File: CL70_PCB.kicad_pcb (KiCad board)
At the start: 2 copper layers, 204 parts, among them J1 AVR-ISP-6, SW1 SW_Push, U1 ATmega32U4-MU, U2 PRTR5V0U2X, Y1 16MHz

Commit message: Realignment footprint
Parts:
- moved C5 52.3 mm to (341.3, 150.0), turned to -90 degrees
- moved C4 47.6 mm to (345.3, 139.8), turned to -90 degrees
- moved C1 44.5 mm to (349.2, 138.9)
- moved C6 41.6 mm to (352.4, 153.2)
- moved C7 37.4 mm to (355.5, 142.9)
- moved C2 34.8 mm to (361.1, 146.8), turned to 0 degrees
- moved C3 34.5 mm to (361.1, 149.2), turned to 0 degrees
- moved RC8 33.2 mm to (342.0, 153.9), turned to 180 degrees
- moved D71 10.3 mm to (377.0, 164.2)
- moved D32 6.20 mm to (337.3, 134.1)
- moved D68 6.20 mm to (327.8, 191.2)
- moved D69 6.20 mm to (346.9, 191.2)
- moved D47 6.16 mm to (330.2, 153.1)
- moved D60 6.10 mm to (346.9, 172.2)
- moved J1 3.27 mm to (356.7, 168.1)
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
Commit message: Add PCB outline
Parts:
- moved C2 0.91 mm to (360.2, 146.8)
- moved C3 0.91 mm to (360.2, 149.2)
- moved Y1 0.91 mm to (355.5, 147.9)
- moved USB1 0.46 mm to (350.1, 95.8)
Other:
- board outline added: 343.8 x 98.1 mm
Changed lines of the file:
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@@
 	(footprint "locallib:C_0603"
 		(layer "B.Cu")
-		(at 361.1 149.225)
+		(at 360.19375 149.225)
 		(descr "Capacitor SMD 0603, reflow soldering, AVX (see smccp.pdf)")
 		(tags "capacitor 0603")
@@
 	(footprint "locallib:C_0603"
 		(layer "B.Cu")
-		(at 361.1 146.84375)
+		(at 360.19375 146.84375)
 		(descr "Capacitor SMD 0603, reflow soldering, AVX (see smccp.pdf)")
 		(tags "capacitor 0603")
@@
 	(footprint "Crystal:Crystal_SMD_3225-4Pin_3.2x2.5mm"
 		(layer "B.Cu")
-		(at 356.45 147.94375 90)
+		(at 355.54375 147.94375 90)
 		(descr "SMD3225/4, Crystal, 3.2x2.5mm package, SMD, generated with kicad-footprint-generator make_crystal.py, http://www.txccrystal.com/images/pdf/7m-accuracy.pdf")
 		(property "Reference" "Y1"
@@
 	(footprint "Type-C:HRO-TYPE-C-31-M-12-Assembly"
 		(layer "B.Cu")
-		(at 350.04375 95.35)
+		(at 350.05 95.805)
 		(property "Reference" "USB1"
 			(at 0 9.25 0)
@@
 		(layer "Dwgs.User")
 	)
+	(gr_arc
+		(start 371.475 146.75)
+		(mid 383.475004 158.750002)
+		(end 371.475 170.75)
+		(stroke
+			(width 0.2)
+			(type default)
+		)
+		(layer "Edge.Cuts")
+	)
+	(gr_arc
+		(start 354.421762 97.2107)
+		(mid 354.983056 97.443195)
+		(end 355.21555 98.004492)
+		(stroke
+			(width 0.2)
+			(type default)
+		)
+		(layer "Edge.Cuts")
+	)
+	(gr_line
+		(start 39.6875 192.88125)
+		(end 39.6875 105.568812)
+		(stroke
+			(width 0.2)
+			(type default)
+		)
+		(layer "Edge.Cuts")
+	)
+	(gr_arc
+		(start 344.87195 98.004592)
+		(mid 345.104451 97.443225)
+		(end 345.665762 97.21078)
+		(stroke
+			(width 0.2)
+			(type default)
+		)
+		(layer "Edge.Cuts")
+	)
+	(gr_arc
+		(start 39.6875 105.568812)
+		(mid 40.384966 103.884975)
+		(end 42.068812 103.1875)
+		(stroke
+			(width 0.2)
+			(type default)
+		)
+		(layer "Edge.Cuts")
+	)
+	(gr_arc
+		(start 369.8875 192.881292)
+		(mid 369.190062 194.565071)
+		(end 367.50625 195.2625)
+		(stroke
+			(width 0.2)
+			(type default)
+		)
+		(layer "Edge.Cuts")
+	)
+	(gr_line
+		(start 345.665762 97.2107)
+		(end 354.421762 97.2107)
+		(stroke
+			(width 0.2)
+			(type default)
+		)
+		(layer "Edge.Cuts")
+	)
+	(gr_arc
+		(start 344.87195 101.599992)
+		(mid 344.406978 102.722523)
+		(end 343.28445 103.1875)
+		(stroke
+			(width 0.2)
+			(type default)
+		)
+		(layer "Edge.Cuts")
+	)
+	(gr_line
+		(start 343.28445 103.1875)
+		(end 42.068812 103.1875)
+		(stroke
+			(width 0.2)
+			(type default)
+		)
+		(layer "Edge.Cuts")
+	)
+	(gr_line
+		(start 369.8875 172.337492)
+		(end 369.8875 192.881292)
+		(stroke
+			(width 0.2)
+			(type default)
+		)
+		(layer "Edge.Cuts")
+	)
+	(gr_line
+		(start 345.665762 97.21078)
+		(end 345.665762 97.2107)
+		(stroke
+			(width 0.2)
+			(type default)
+		)
+		(layer "Edge.Cuts")
+	)
+	(gr_arc
+		(start 356.803062 103.1875)
+		(mid 355.680523 102.722528)
+		(end 355.21555 101.599992)
+		(stroke
+			(width 0.2)
+			(type default)
+		)
+		(layer "Edge.Cuts")
+	)
+	(gr_arc
+		(start 367.506262 103.1875)
+		(mid 369.190071 103.884945)
+		(end 369.8875 105.56875)
+		(stroke
+			(width 0.2)
+			(type default)
+		)
+		(layer "Edge.Cuts")
+	)
+	(gr_arc
+		(start 371.475 146.75)
+		(mid 370.352441 146.285046)
+		(end 369.8875 145.1625)
+		(stroke
+			(width 0.2)
+			(type default)
+		)
+		(layer "Edge.Cuts")
+	)
+	(gr_line
+		(start 344.87195 101.599992)
+		(end 344.87195 98.004592)
+		(stroke
+			(width 0.2)
+			(type default)
+		)
+		(layer "Edge.Cuts")
+	)
+	(gr_line
+		(start 42.068762 195.2625)
+		(end 367.50625 195.2625)
+		(stroke
+			(width 0.2)
+			(type default)
+		)
+		(layer "Edge.Cuts")
+	)
+	(gr_line
+		(start 355.21555 98.004492)
+		(end 355.21555 101.599992)
+		(stroke
+			(width 0.2)
+			(type default)
+		)
+		(layer "Edge.Cuts")
+	)
+	(gr_arc
+		(start 42.068762 195.2625)
+		(mid 40.384954 194.565047)
+		(end 39.6875 192.88125)
+		(stroke
+			(width 0.2)
+			(type default)
+		)
+		(layer "Edge.Cuts")
+	)
+	(gr_arc
+		(start 369.8875 172.337492)
+		(mid 370.352467 171.214976)
+		(end 371.475 170.75)
+		(stroke
+			(width 0.2)
+			(type default)
+		)
+		(layer "Edge.Cuts")
+	)
+	(gr_line
+		(start 367.506262 103.1875)
+		(end 356.803062 103.1875)
+		(stroke
+			(width 0.2)
+			(type default)
+		)
+		(layer "Edge.Cuts")
+	)
+	(gr_line
+		(start 369.8875 105.56875)
+		(end 369.8875 145.1625)
+		(stroke
+			(width 0.2)
+			(type default)
+		)
+		(layer "Edge.Cuts")
+	)
 	(group ""
 		(members "01f0b98f-9fbf-4339-9750-24d2992556fd" "0355ff27-1e74-4531-91ec-7afcd7ec99a2"
@@
 		)
 	)
+	(group ""
+		(members "0e2a9951-a378-4da8-98fe-729fd5110501" "11c98efb-e5c4-4a83-9d8d-b93e626b395c"
+			"19e8fbd3-0d80-4f89-bcad-f88af3cd8026" "2a881e81-64bd-49b1-8f18-b7fc72406794"
+			"2c628242-99f6-44d3-804e-fae6e092cd84" "36ff1723-645c-4ea2-a89e-666fb6f61650"
+			"40e42480-0976-4067-8680-fe6dd074dff7" "46f23a6b-3d0c-4e92-805b-4b3b9c2d146e"
+			"47799a47-71c1-41d2-be0c-02f1f8502c5b" "6a57dcbe-f917-4bf4-afba-9318e853d4c9"
+			"6dfccded-3a9c-4300-a0bb-f29846b9b758" "7f1c7e5f-c4c1-428b-bafd-2ee28e34fea0"
+			"8342ee14-e821-4a54-89ae-72e6da792c9f" "b58aadb1-8298-497d-8d19-9d3c9efc98b3"
+			"bbc2a745-2ae9-4e90-8fd2-8394d0d31e88" "bf7335ba-ab35-49f0-846f-eec9758f1bc8"
+			"ca3899e7-4a94-421b-8d8c-8840a08a6e91" "df78106b-4ed4-4e74-bcb2-cc24398d9495"
+			"e9bb1a92-d6f3-49a2-afdc-1b0c10f2b2ad" "ee82f6a7-5d3c-43cf-abe7-82fa5f20290f"
+			"f653473b-249b-42f0-b5a5-de18ca18a995"
+		)
+	)

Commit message: Add wiring
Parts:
- RC1, RC2: value 22 -> 22k
- RLED1, RLED2, RLED3: value 1k -> 330
- moved SW1 19.4 mm to (361.9, 140.8), turned to 0 degrees
- moved D71 15.6 mm to (365.8, 153.4)
- moved RC3 14.2 mm to (355.4, 139.8), turned to 0 degrees
- moved CRGB12 12.6 mm to (187.2, 176.3)
- moved CRGB5 12.4 mm to (187.0, 119.9)
- moved CRGB8 12.3 mm to (61.5, 120.2)
- moved CRGB7 12.2 mm to (103.5, 119.9)
- moved CRGB11 12.2 mm to (144.8, 177.4)
- moved CRGB6 12.2 mm to (144.8, 119.9)
- moved CRGB10 12.0 mm to (103.2, 177.1)
- moved J1 5.12 mm to (356.7, 163.0)
- moved C2 2.43 mm to (360.7, 149.2)
- moved C3 2.42 mm to (360.6, 146.8)
- moved C8 1.64 mm to (365.6, 171.5)
- moved C9 1.55 mm to (365.6, 169.9)
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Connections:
- RC4 pad 1: Net-(U1-PD0) -> Net-(U1-PD2)
- RC4 pad 2: RESW_A -> RESW_B
- RC5 pad 2: RESW_B -> RESW_A
- S47 pad 1: COL8 -> COL7
- U1 pad 18: Net-(U1-PD0) -> ROW7
- U1 pad 20: ROW9 -> Net-(U1-PD2)
- U1 pad 22: ROW7 -> ROW9
- U1 pad 26: ROW5 -> ROW4
- U1 pad 27: ROW4 -> ROW5
- U1 pad 28: ROW3 -> ROW2
- U1 pad 29: ROW2 -> ROW3
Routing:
- net GND: track 0.00 -> 912.2 mm, vias 0 -> 6
- net +5V: track 0.00 -> 788.4 mm, vias 0 -> 12
- net COL2: track 0.00 -> 469.4 mm, vias 0 -> 1
- net COL1: track 0.00 -> 462.7 mm, vias 0 -> 2
- net COL3: track 0.00 -> 432.4 mm, vias 0 -> 2
- net COL0: track 0.00 -> 421.0 mm, vias 0 -> 1
- net ROW0: track 0.00 -> 400.1 mm, vias 0 -> 4
- net COL4: track 0.00 -> 375.7 mm, vias 0 -> 2
- net ROW3: track 0.00 -> 364.2 mm, vias 0 -> 2
- net ROW1: track 0.00 -> 355.6 mm, vias 0 -> 2
- net ROW8: track 0.00 -> 353.8 mm
- net SLOCK_IND: track 0.00 -> 353.0 mm, vias 0 -> 2
- net CAPS_IND: track 0.00 -> 349.4 mm, vias 0 -> 2
- net LAYER_IND: track 0.00 -> 342.4 mm, vias 0 -> 2
- net ROW2: track 0.00 -> 340.6 mm
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
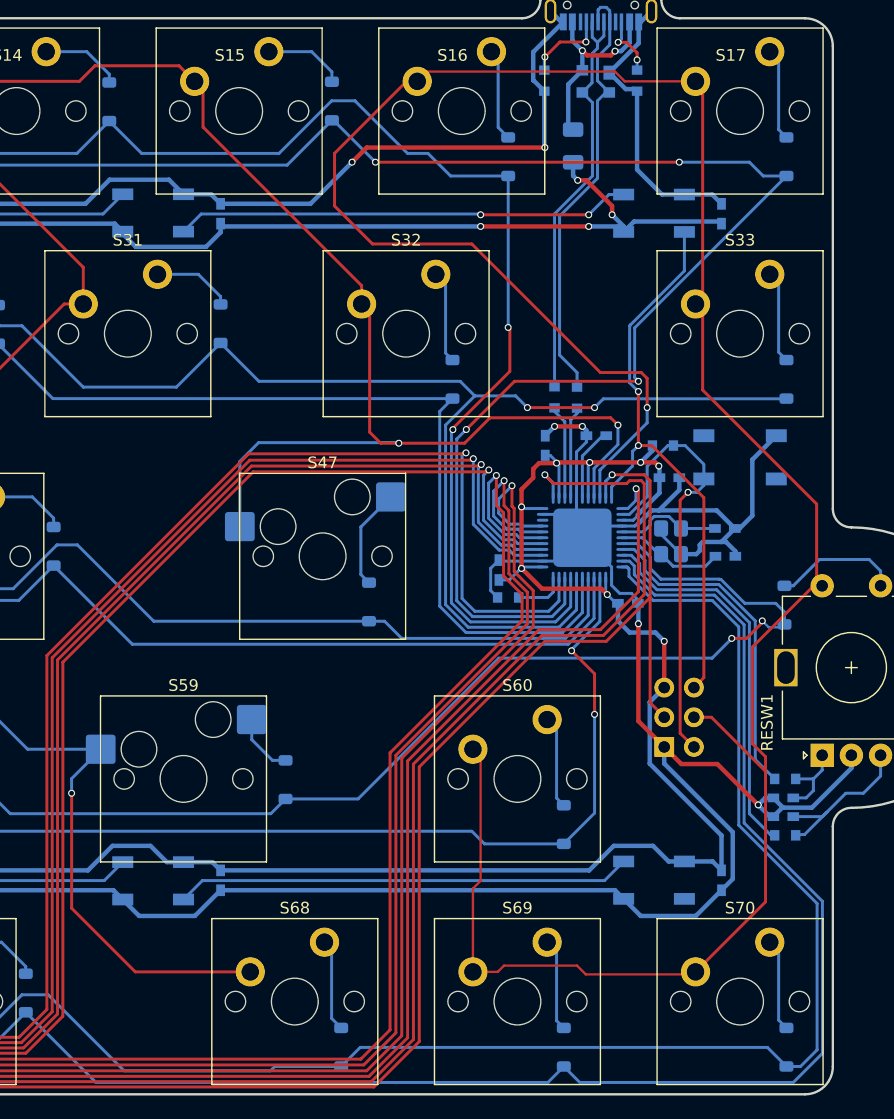
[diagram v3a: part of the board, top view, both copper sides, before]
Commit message: Add graphic sorder mask
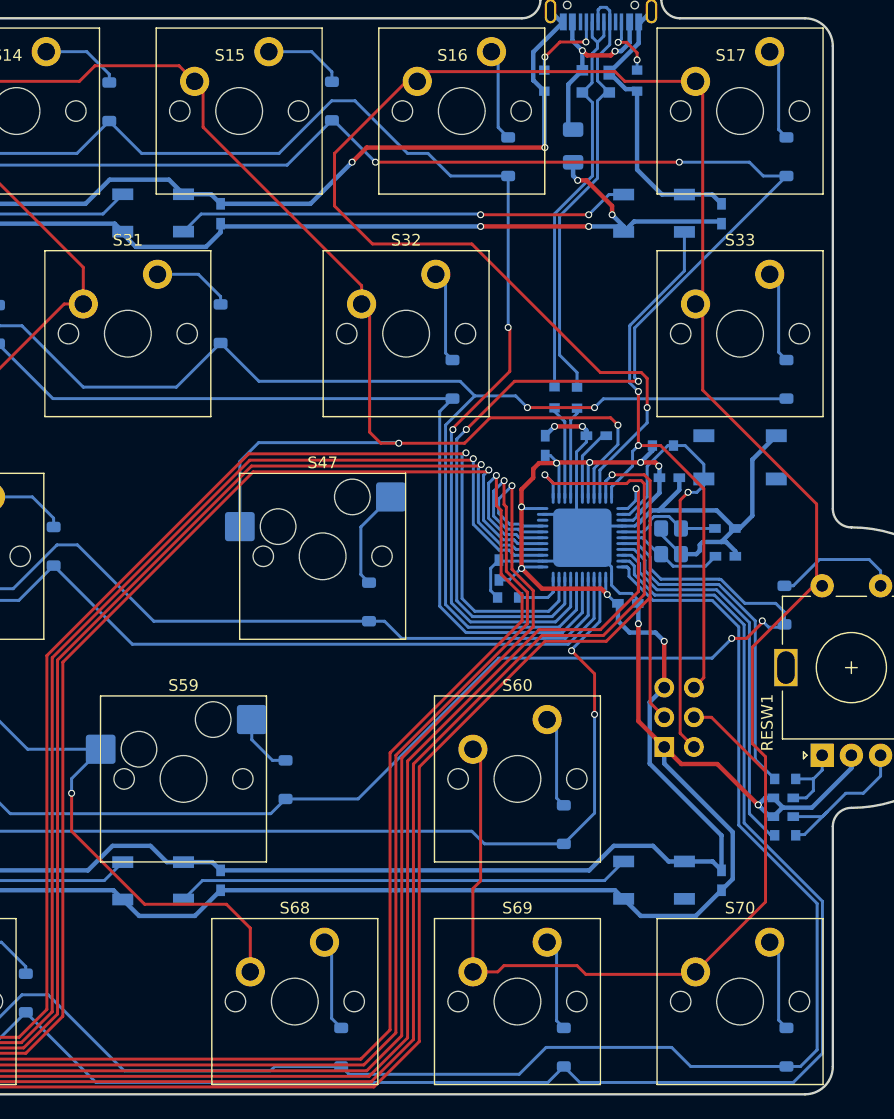
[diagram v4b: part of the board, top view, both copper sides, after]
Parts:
- added G***: LOGO, Graphics:SURVEY_CORPS, F.Cu at (309.5, 187.3)
- added G***: LOGO, Graphics:PCB_INFO, B.Cu at (269.9, 158.2)
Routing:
- net COL7: track 216.5 -> 214.8 mm
- net ROW9: track 334.8 -> 335.4 mm
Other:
- board text added: "+"
- board text added: "-"

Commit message: Add production files
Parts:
- RC1, RC2: value 22k -> 22
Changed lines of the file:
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@@
 		(tenting front back)
 		(pcbplotparams
-			(layerselection 0x00000000_00000000_55555555_5755f5ff)
+			(layerselection 0x00000000_00000000_55555555_5755f5df)
 			(plot_on_all_layers_selection 0x00000000_00000000_00000000_00000000)
 			(disableapertmacros no)
@@
 			(outputformat 1)
 			(mirror no)
-			(drillshape 1)
+			(drillshape 0)
 			(scaleselection 1)
-			(outputdirectory "")
+			(outputdirectory "Production/Gerber/")
 		)
 	)
@@
 			)
 		)
-		(property "Value" "22k"
+		(property "Value" "22"
 			(at 0 -1.5 90)
 			(layer "B.Fab")
@@
 			)
 		)
-		(property "Value" "22k"
+		(property "Value" "22"
 			(at 0 -1.5 90)
 			(layer "B.Fab")
@@
 		(start 61.11875 188.9125)
 		(end 62.4125 188.9125)
-		(width 0.254)
+		(width 0.381)
 		(layer "B.Cu")
 		(net 89)
@@
 		(start 53.6875 182.5625)
 		(end 50 178.875)
-		(width 0.254)
+		(width 0.381)
 		(layer "B.Cu")
 		(net 92)
@@
 		(start 50 175.73)
 		(end 48.895 174.625)
-		(width 0.254)
+		(width 0.381)
 		(layer "B.Cu")
 		(net 92)
@@
 		(start 50 178.875)
 		(end 50 175.73)
-		(width 0.254)
+		(width 0.381)
 		(layer "B.Cu")
 		(net 92)
@@
 		(start 59.31875 182.5625)
 		(end 53.6875 182.5625)
-		(width 0.254)
+		(width 0.381)
 		(layer "B.Cu")
 		(net 92)
@@
 		(start 59.31875 185.7375)
 		(end 53.66375 185.7375)
-		(width 0.254)
+		(width 0.381)
 		(layer "B.Cu")
 		(net 93)
@@
 		(start 53.66375 185.7375)
 		(end 48.895 180.96875)
-		(width 0.254)
+		(width 0.381)
 		(layer "B.Cu")
 		(net 93)
@@
 		(start 53.6625 188.9125)
 		(end 52.0625 187.3125)
-		(width 0.254)
+		(width 0.381)
 		(layer "B.Cu")
 		(net 94)
@@
 		(start 52.0625 187.3125)
 		(end 48.895 187.3125)
-		(width 0.254)
+		(width 0.381)
 		(layer "B.Cu")
 		(net 94)
@@
 		(start 59.31875 188.9125)
 		(end 53.6625 188.9125)
-		(width 0.254)
+		(width 0.381)
 		(layer "B.Cu")
 		(net 94)
@@
 		(start 61.11875 182.5625)
 		(end 62.4375 182.5625)
-		(width 0.254)
+		(width 0.381)
 		(layer "B.Cu")
 		(net 122)
@@
 		(start 61.11875 185.7375)
 		(end 62.4875 185.7375)
-		(width 0.254)
+		(width 0.381)
 		(layer "B.Cu")
 		(net 123)
@@
 	)
 	(segment
-		(start 341.75 142.767359)
-		(end 341.75 144.8)
-		(width 0.254)
-		(layer "F.Cu")
-		(net 125)
-	)
-	(segment
 		(start 68.2125 108)
 		(end 77 108)
@@
 	)
 	(segment
-		(start 332.5 166.25)
-		(end 332.5 190)
+		(start 332.5 190)
+		(end 329.75 192.75)
 		(width 0.254)
 		(layer "F.Cu")
@@
 	)
 	(segment
-		(start 329.75 192.75)
-		(end 96.5 192.75)
+		(start 343.75 152.3)
+		(end 343.75 155)
 		(width 0.254)
 		(layer "F.Cu")
@@
 	)
 	(segment
-		(start 341.760686 142.756673)
-		(end 341.75 142.767359)
+		(start 94.5 190.75)
+		(end 94.5 185.46375)
+		(width 0.254)
+		(layer "F.Cu")
+		(net 125)
+	)
+	(segment
+		(start 94.5 185.46375)
+		(end 93.82125 184.785)
 		(width 0.254)
 		(layer "F.Cu")
@@
 	)
 	(segment
-		(start 93.82125 190.07125)
-		(end 93.82125 184.785)
+		(start 96.5 192.75)
+		(end 94.5 190.75)
+		(width 0.254)
+		(layer "F.Cu")
+		(net 125)
+	)
+	(segment
+		(start 341.760686 142.756673)
+		(end 341.75 142.767359)
 		(width 0.254)
 		(layer "F.Cu")
@@
 	)
 	(segment
-		(start 96.5 192.75)
-		(end 93.82125 190.07125)
+		(start 341.75 142.767359)
+		(end 341.75 144.8)
 		(width 0.254)
 		(layer "F.Cu")
@@
 	)
 	(segment
-		(start 341.95 145)
-		(end 341.95 150.5)
+		(start 77.75 107.25)
+		(end 85.3425 107.25)
 		(width 0.254)
 		(layer "F.Cu")
@@
 	)
 	(segment
-		(start 341.95 150.5)
-		(end 343.75 152.3)
+		(start 84.5 184.25)
+		(end 85.035 184.785)
 		(width 0.254)
 		(layer "F.Cu")
@@
 	)
 	(segment
-		(start 332.5 190)
-		(end 329.75 192.75)
+		(start 70 168.5)
+		(end 68.5 170)
 		(width 0.254)
 		(layer "F.Cu")
@@
 	)
 	(segment
-		(start 77.75 107.25)
-		(end 85.3425 107.25)
+		(start 341.75 144.8)
+		(end 341.95 145)
 		(width 0.254)
 		(layer "F.Cu")
@@
 	)
 	(segment
-		(start 84.5 184.25)
-		(end 85.035 184.785)
+		(start 85.3425 107.25)
+		(end 86.6775 108.585)
 		(width 0.254)
 		(layer "F.Cu")
@@
 	)
 	(segment
-		(start 70 168.5)
-		(end 68.5 170)
+		(start 77 108)
+		(end 77.75 107.25)
 		(width 0.254)
 		(layer "F.Cu")
@@
 	)
 	(segment
-		(start 85.3425 107.25)
-		(end 86.6775 108.585)
+		(start 72.39 128.89)
+		(end 73.25 129.75)
 		(width 0.254)
 		(layer "F.Cu")
@@
 	)
 	(segment
-		(start 77 108)
-		(end 77.75 107.25)
+		(start 73.25 145.16375)
+		(end 74.77125 146.685)
 		(width 0.254)
 		(layer "F.Cu")
@@
 	)
 	(segment
-		(start 343.75 152.3)
-		(end 343.75 155)
+		(start 70.54375 184.25)
+		(end 84.5 184.25)
 		(width 0.254)
 		(layer "F.Cu")
@@
 	)
 	(segment
-		(start 72.39 128.89)
-		(end 73.25 129.75)
+		(start 72.39 127.635)
+		(end 72.39 128.89)
 		(width 0.254)
 		(layer "F.Cu")
@@
 	)
 	(segment
-		(start 341.75 144.8)
-		(end 341.95 145)
+		(start 332.5 166.25)
+		(end 332.5 190)
 		(width 0.254)
 		(layer "F.Cu")
@@
 	)
 	(segment
-		(start 73.25 145.16375)
-		(end 74.77125 146.685)
+		(start 91.885 127.635)
+		(end 96.2025 127.635)
 		(width 0.254)
 		(layer "F.Cu")
@@
 	)
 	(segment
-		(start 70.54375 184.25)
-		(end 84.5 184.25)
+		(start 68.5 170)
+		(end 68.5 183.27625)
 		(width 0.254)
 		(layer "F.Cu")
@@
 	)
 	(segment
-		(start 72.39 127.635)
-		(end 72.39 128.89)
+		(start 329.75 192.75)
+		(end 96.5 192.75)
 		(width 0.254)
 		(layer "F.Cu")
@@
 	)
 	(segment
-		(start 91.885 127.635)
-		(end 96.2025 127.635)
+		(start 341.95 145)
+		(end 341.95 150.5)
 		(width 0.254)
 		(layer "F.Cu")
@@
 	)
 	(segment
-		(start 68.5 170)
-		(end 68.5 183.27625)
+		(start 341.95 150.5)
+		(end 343.75 152.3)
 		(width 0.254)
 		(layer "F.Cu")
